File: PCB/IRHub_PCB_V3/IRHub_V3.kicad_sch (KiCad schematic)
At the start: 66 parts, among them J2 USB_C_Receptacle_USB2.0_16P, Q1 UMH3N, Q2 AO3400A, Q3 AO3400A, U1 ESP-12F, U2 CH340C, U3 AMS1117-3.3, U4 TSOP382xx, U5 ME6211C33M5

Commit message: complete schematic i think ?
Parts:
- removed OLED1: Conn_01x04_Pin, Connector_PinHeader_2.54mm:PinHeader_1x04_P2.54mm_Vertical, symbol Connector:Conn_01x04_Pin
- added 5V1: VCC, TestPoint:TestPoint_Pad_D2.0mm, symbol Connector:TestPoint
- added DispTouch: DispTouch, Connector_JST:JST_SH_BM06B-SRSS-TB_1x06-1MP_P1.00mm_Vertical, symbol Connector:Conn_01x06_Socket
- added TP9: 3V3, TestPoint:TestPoint_Pad_D2.0mm, symbol Connector:TestPoint
- added T_D+1: D+, TestPoint:TestPoint_Pad_D2.0mm, symbol Connector:TestPoint
- added T_D-1: D-, TestPoint:TestPoint_Pad_D2.0mm, symbol Connector:TestPoint
- added T_D6: D6, TestPoint:TestPoint_Pad_D2.0mm, symbol Connector:TestPoint
- added T_D7: D7, TestPoint:TestPoint_Pad_D2.0mm, symbol Connector:TestPoint
- added T_GND1: GND, TestPoint:TestPoint_Pad_D2.0mm, symbol Connector:TestPoint
- added T_RX1: RX, TestPoint:TestPoint_Pad_D2.0mm, symbol Connector:TestPoint
- added T_TX1: TX, TestPoint:TestPoint_Pad_D2.0mm, symbol Connector:TestPoint
- LS1: footprint CMT-7525-80-SMT-TR:XDCR_CMT-7525-80-SMT-TR -> CMT-7525:XDCR_CMT-7525-80-SMT-TR
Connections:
- net +3.3V: now also DispTouch.2 (Pin_2), TP9.1
- net +5V: now also 5V1.1
- net D+: now also T_D+1.1
- net D-: now also T_D-1.1
- net D0: now also DispTouch.5 (Pin_5)
- net D1: now also DispTouch.3 (Pin_3)
- net D2: now also DispTouch.4 (Pin_4)
- net D6: now also T_D6.1
- net D7: now also T_D7.1
- net GND: now also DispTouch.1 (Pin_1), DispTouch.6 (Pin_6), T_GND1.1
- net RX: now also T_RX1.1
- net TX: now also T_TX1.1
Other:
- moved on the sheet: D31, D32, D33, D34, D35, D36, D37, D38, R10, R11, R12, R13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

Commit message: final design i think
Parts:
- removed D32, D33, D34, D35, D36, D37, D38: IR204A, LED_THT:LED_D3.0mm_IRBlack, symbol LED:IR204A
- added IR_L2, IR_L3, IR_L4, IR_L5, IR_L6, IR_L7, IR_L8: IR204A, LED_THT:LED_D3.0mm_IRBlack, symbol LED:IR204A
- added R16, R17, R18: 12000, Resistor_SMD:R_1206_3216Metric_Pad1.30x1.75mm_HandSolder, symbol Device:R
- added SW1: SW_Push, Button_Switch_SMD:SW_SPST_TS-1088-xR020, symbol Switch:SW_Push
- BZR1: renamed from LS1; value CMT-7525-80-SMT-TR -> CMT-7525
- R6: value 5100 -> 12000
- renumbered U3 to AMS1117, U2 to CH340C1, DispTouch to DispTouch1, U1 to ESP1, D31 to IR_L1, U4 to IR_RECV1, U5 to ME6211, Q3 to MFT1, Q2 to MFT2, J2 to USB1
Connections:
- net +3.3V: now also R17.2, R18.2
- net D3: now also R15.2; no longer R15.1
- net D4: now also R18.1
- net D8: now also R16.1
- net GND: now also R16.2, SW1.2
- net IR_GND: now also IR_L2.1 (K), IR_L3.1 (K), IR_L4.1 (K), IR_L5.1 (K), IR_L6.1 (K), IR_L7.1 (K), IR_L8.1 (K)
- net RST: now also R17.1, SW1.1
- net at R13.1: now also IR_L7.2 (A)
- net at R8.1: now also IR_L2.2 (A)
- net at R11.1: now also IR_L5.2 (A)
- net at R10.1: now also IR_L4.2 (A)
- net at R9.1: now also IR_L3.2 (A)
- net at MFT1.1 (G): now also R15.1; no longer R15.2
- net at R12.1: now also IR_L6.2 (A)
- net at R14.1: now also IR_L8.2 (A)
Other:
- moved on the sheet: 5V1, AMS1117, BZR1, C3, C4, CH340C1, DispTouch1, ESP1, IR_L1, IR_RECV1, ME6211, MFT1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

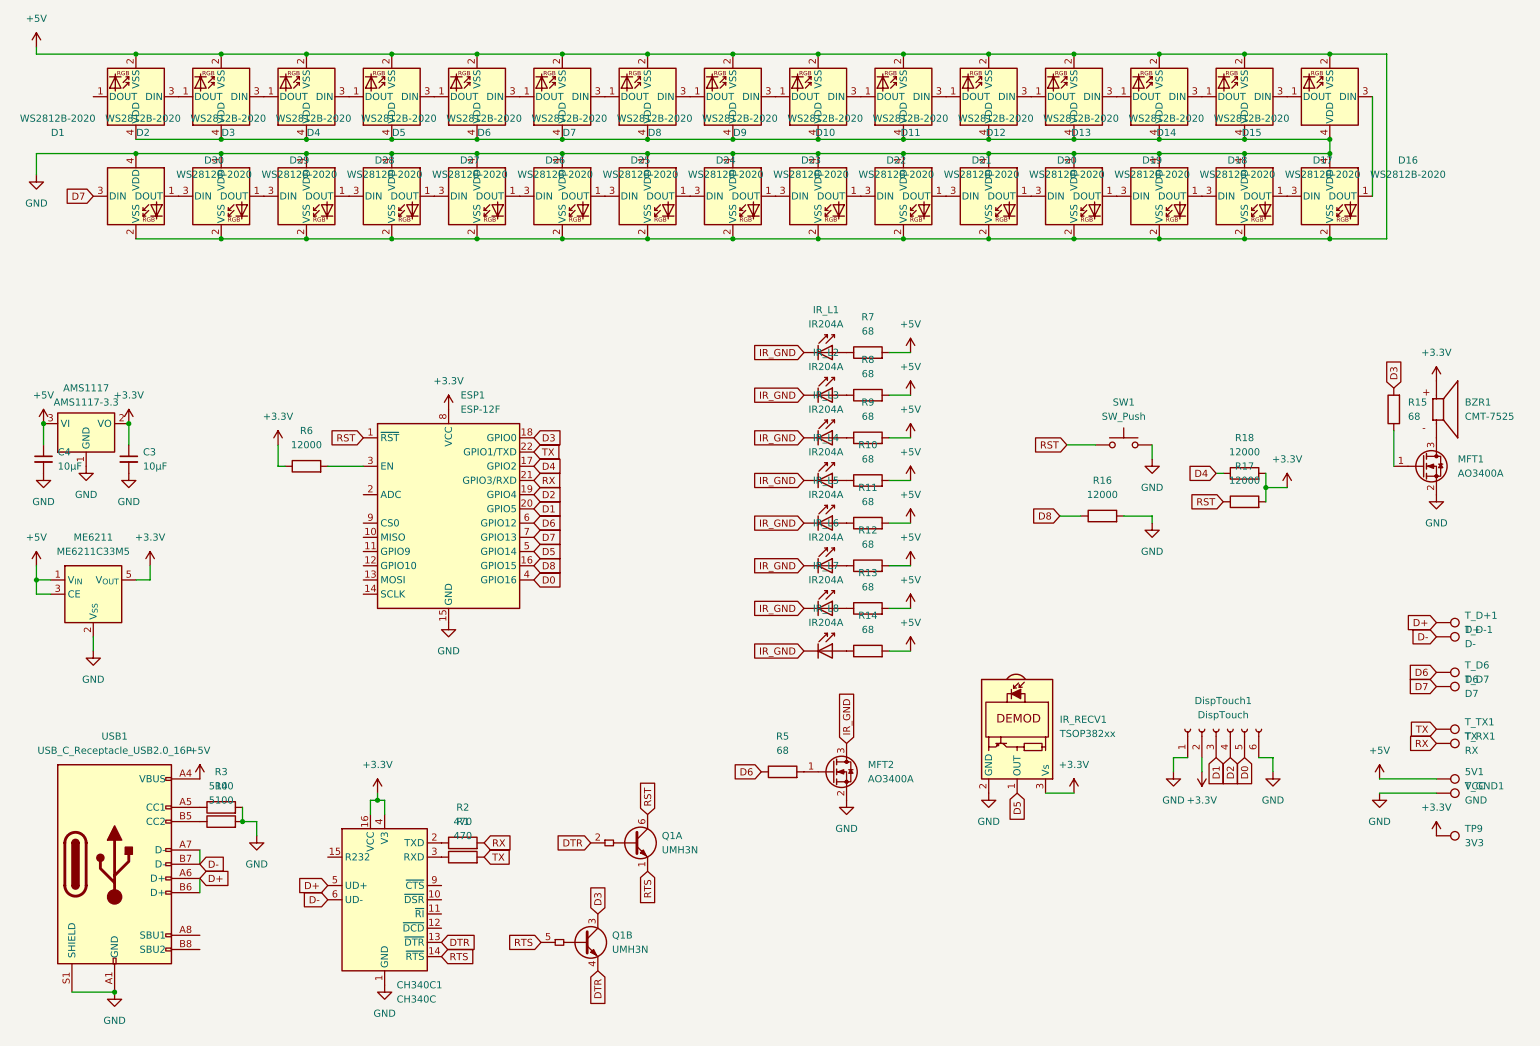
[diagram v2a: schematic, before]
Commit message: added haptics
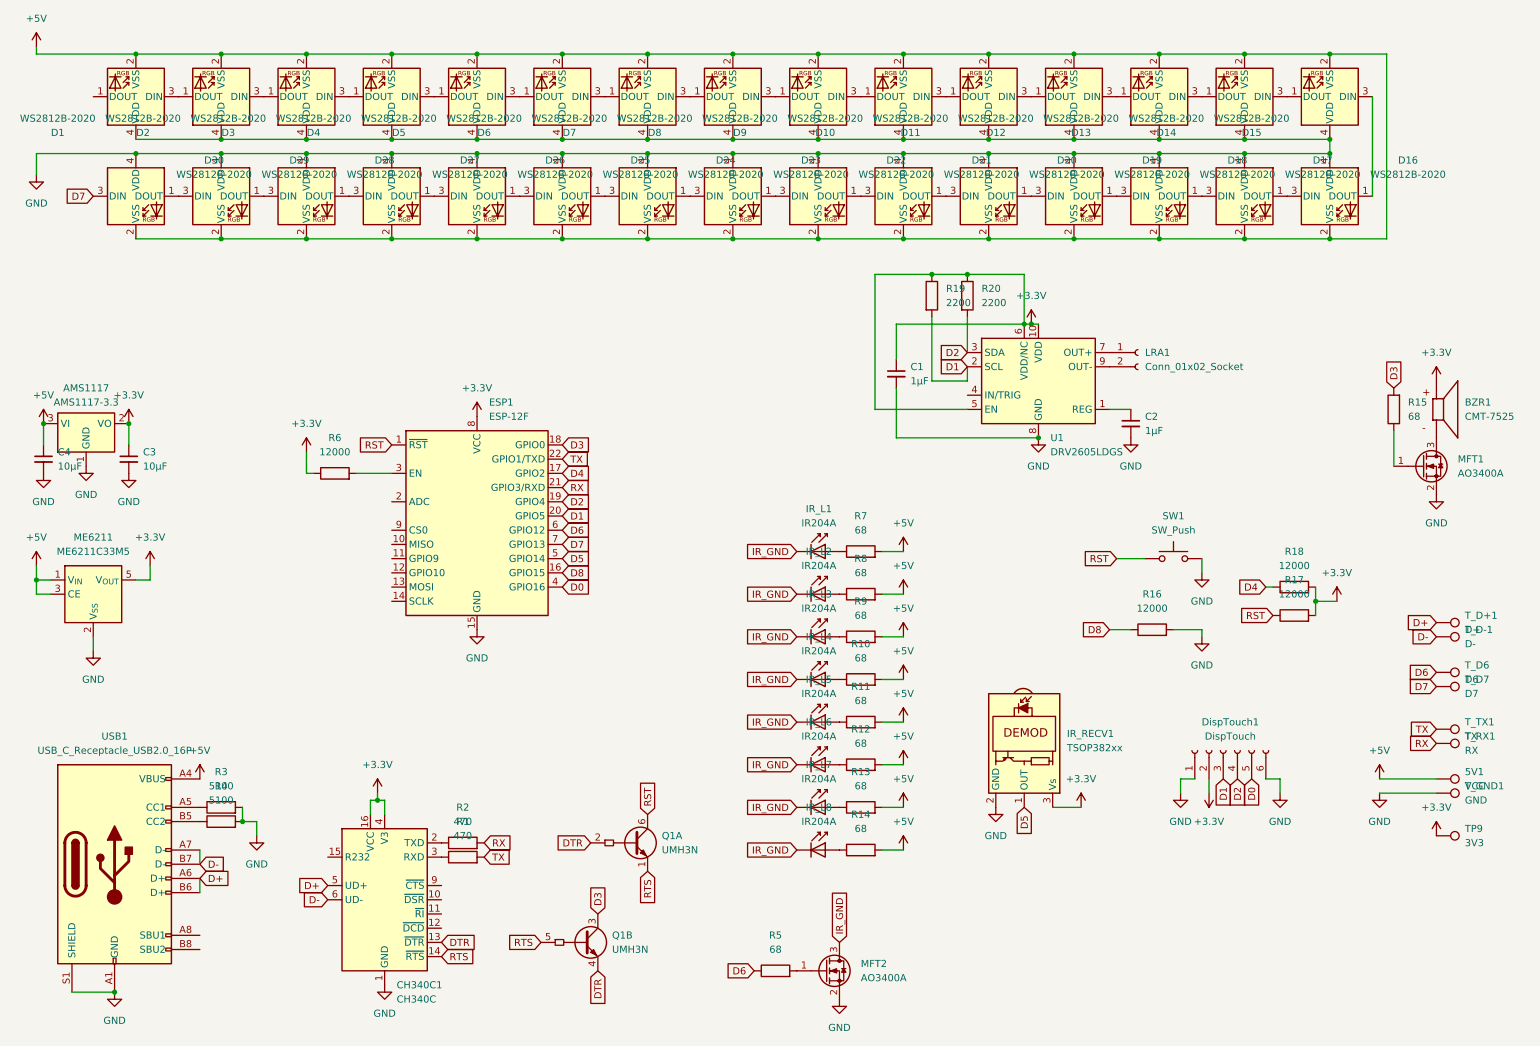
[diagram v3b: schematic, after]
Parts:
- added C1, C2: 1µF, Capacitor_SMD:C_0805_2012Metric_Pad1.18x1.45mm_HandSolder, symbol Device:C_Small
- added LRA1: Conn_01x02_Socket, Connector_PinHeader_2.00mm:PinHeader_1x02_P2.00mm_Vertical, symbol Connector:Conn_01x02_Socket
- added R19, R20: 2200, Resistor_SMD:R_0805_2012Metric_Pad1.20x1.40mm_HandSolder, symbol Device:R
- added U1: DRV2605LDGS, Package_SO:VSSOP-10_3x3mm_P0.5mm, symbol Driver_Haptic:DRV2605LDGS
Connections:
- net +3.3V: now also C1.1, R19.1, R20.1, U1.10 (VDD), U1.5 (EN), U1.6 (VDD/NC)
- net D1: now also R19.2, U1.2 (SCL)
- net D2: now also R20.2, U1.3 (SDA)
- net GND: now also C1.2, C2.2, U1.8 (GND)
- new net: C2.1, U1.1 (REG)
- new net: LRA1.1 (Pin_1), U1.7 (OUT+)
- new net: LRA1.2 (Pin_2), U1.9 (OUT-)
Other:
- moved on the sheet: DispTouch1, ESP1, IR_L1, IR_L2, IR_L3, IR_L4, IR_L5, IR_L6, IR_L7, IR_L8, IR_RECV1, MFT2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

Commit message: power pcb done
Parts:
- 5V1, TP9, T_D+1, T_D-1, T_D6, T_D7, T_GND1, T_RX1, T_TX1: footprint TestPoint:TestPoint_Pad_D2.0mm -> TestPoint:TestPoint_Pad_D1.0mm
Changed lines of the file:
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@@
 			)
 		)
-		(property "Footprint" "TestPoint:TestPoint_Pad_D2.0mm"
+		(property "Footprint" "TestPoint:TestPoint_Pad_D1.0mm"
 			(at 267.97 156.21 0)
 			(effects
@@
 			)
 		)
-		(property "Footprint" "TestPoint:TestPoint_Pad_D2.0mm"
+		(property "Footprint" "TestPoint:TestPoint_Pad_D1.0mm"
 			(at 267.97 130.81 0)
 			(effects
@@
 			)
 		)
-		(property "Footprint" "TestPoint:TestPoint_Pad_D2.0mm"
+		(property "Footprint" "TestPoint:TestPoint_Pad_D1.0mm"
 			(at 267.97 149.86 0)
 			(effects
@@
 			)
 		)
-		(property "Footprint" "TestPoint:TestPoint_Pad_D2.0mm"
+		(property "Footprint" "TestPoint:TestPoint_Pad_D1.0mm"
 			(at 267.97 128.27 0)
 			(effects
@@
 			)
 		)
-		(property "Footprint" "TestPoint:TestPoint_Pad_D2.0mm"
+		(property "Footprint" "TestPoint:TestPoint_Pad_D1.0mm"
 			(at 267.97 147.32 0)
 			(effects
@@
 			)
 		)
-		(property "Footprint" "TestPoint:TestPoint_Pad_D2.0mm"
+		(property "Footprint" "TestPoint:TestPoint_Pad_D1.0mm"
 			(at 267.97 166.37 0)
 			(effects
@@
 			)
 		)
-		(property "Footprint" "TestPoint:TestPoint_Pad_D2.0mm"
+		(property "Footprint" "TestPoint:TestPoint_Pad_D1.0mm"
 			(at 267.97 158.75 0)
 			(effects
@@
 			)
 		)
-		(property "Footprint" "TestPoint:TestPoint_Pad_D2.0mm"
+		(property "Footprint" "TestPoint:TestPoint_Pad_D1.0mm"
 			(at 267.97 137.16 0)
 			(effects
@@
 			)
 		)
-		(property "Footprint" "TestPoint:TestPoint_Pad_D2.0mm"
+		(property "Footprint" "TestPoint:TestPoint_Pad_D1.0mm"
 			(at 267.97 139.7 0)
 			(effects

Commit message: finished placement
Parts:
- removed ME6211: ME6211C33M5, Package_TO_SOT_SMD:SOT-23-5, symbol Regulator_Linear:ME6211C33M5
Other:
- moved on the sheet: AMS1117, C3, C4

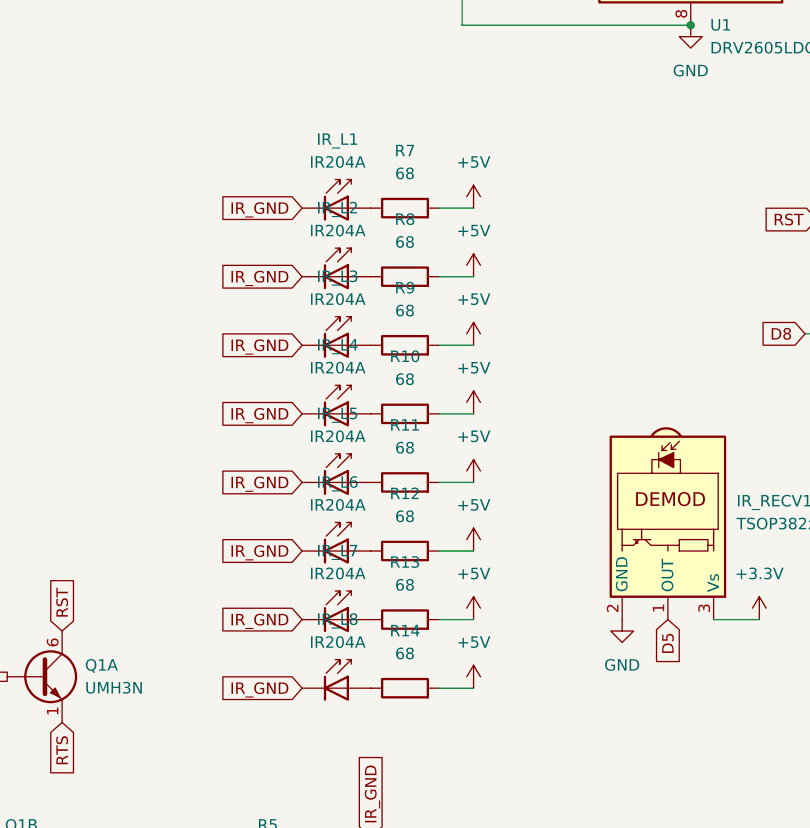
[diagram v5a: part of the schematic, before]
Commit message: update resistor values
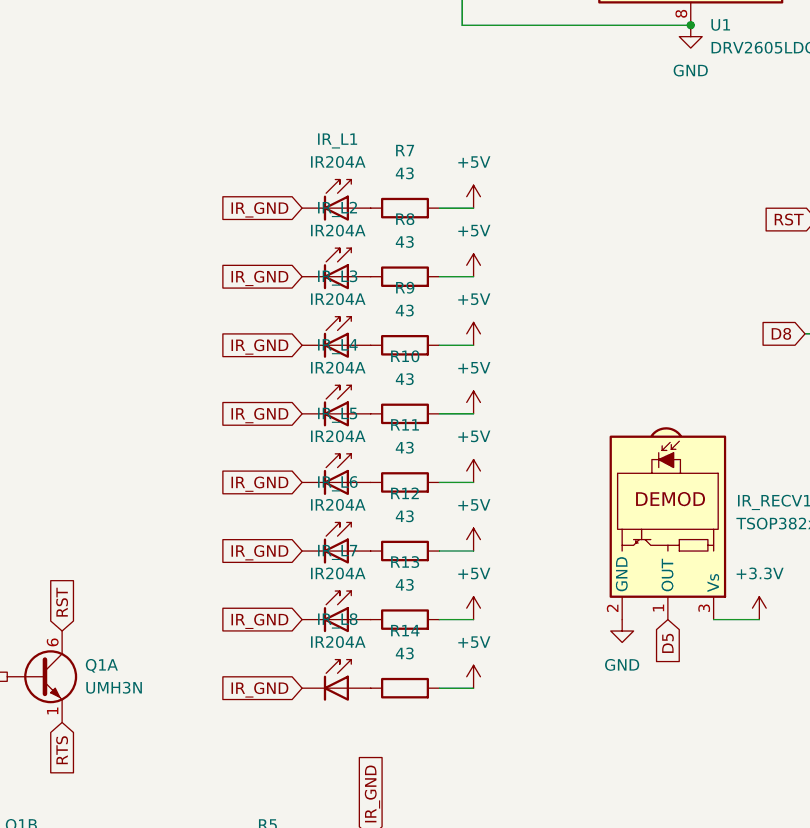
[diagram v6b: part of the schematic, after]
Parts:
- R10, R11, R12, R13, R14, R7, R8, R9: value 68 -> 43; footprint Resistor_SMD:R_1206_3216Metric_Pad1.30x1.75mm_HandSolder -> Resistor_SMD:R_1210_3225Metric_Pad1.30x2.65mm_HandSolder
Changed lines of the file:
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@@
 			)
 		)
-		(property "Value" "68"
+		(property "Value" "43"
 			(at 165.1 137.16 90)
 			(effects
@@
 			)
 		)
-		(property "Footprint" "Resistor_SMD:R_1206_3216Metric_Pad1.30x1.75mm_HandSolder"
+		(property "Footprint" "Resistor_SMD:R_1210_3225Metric_Pad1.30x2.65mm_HandSolder"
 			(at 165.1 142.748 90)
 			(effects
@@
 			)
 		)
-		(property "Value" "68"
+		(property "Value" "43"
 			(at 165.1 121.92 90)
 			(effects
@@
 			)
 		)
-		(property "Footprint" "Resistor_SMD:R_1206_3216Metric_Pad1.30x1.75mm_HandSolder"
+		(property "Footprint" "Resistor_SMD:R_1210_3225Metric_Pad1.30x2.65mm_HandSolder"
 			(at 165.1 127.508 90)
 			(effects
@@
 			)
 		)
-		(property "Value" "68"
+		(property "Value" "43"
 			(at 165.1 144.78 90)
 			(effects
@@
 			)
 		)
-		(property "Footprint" "Resistor_SMD:R_1206_3216Metric_Pad1.30x1.75mm_HandSolder"
+		(property "Footprint" "Resistor_SMD:R_1210_3225Metric_Pad1.30x2.65mm_HandSolder"
 			(at 165.1 150.368 90)
 			(effects
@@
 			)
 		)
-		(property "Value" "68"
+		(property "Value" "43"
 			(at 165.1 106.68 90)
 			(effects
@@
 			)
 		)
-		(property "Footprint" "Resistor_SMD:R_1206_3216Metric_Pad1.30x1.75mm_HandSolder"
+		(property "Footprint" "Resistor_SMD:R_1210_3225Metric_Pad1.30x2.65mm_HandSolder"
 			(at 165.1 112.268 90)
 			(effects
@@
 			)
 		)
-		(property "Value" "68"
+		(property "Value" "43"
 			(at 165.1 152.4 90)
 			(effects
@@
 			)
 		)
-		(property "Footprint" "Resistor_SMD:R_1206_3216Metric_Pad1.30x1.75mm_HandSolder"
+		(property "Footprint" "Resistor_SMD:R_1210_3225Metric_Pad1.30x2.65mm_HandSolder"
 			(at 165.1 157.988 90)
 			(effects
@@
 			)
 		)
-		(property "Value" "68"
+		(property "Value" "43"
 			(at 165.1 129.54 90)
 			(effects
@@
 			)
 		)
-		(property "Footprint" "Resistor_SMD:R_1206_3216Metric_Pad1.30x1.75mm_HandSolder"
+		(property "Footprint" "Resistor_SMD:R_1210_3225Metric_Pad1.30x2.65mm_HandSolder"
 			(at 165.1 135.128 90)
 			(effects
@@
 			)
 		)
-		(property "Value" "68"
+		(property "Value" "43"
 			(at 165.1 114.3 90)
 			(effects
@@
 			)
 		)
-		(property "Footprint" "Resistor_SMD:R_1206_3216Metric_Pad1.30x1.75mm_HandSolder"
+		(property "Footprint" "Resistor_SMD:R_1210_3225Metric_Pad1.30x2.65mm_HandSolder"
 			(at 165.1 119.888 90)
 			(effects
@@
 			)
 		)
-		(property "Value" "68"
+		(property "Value" "43"
 			(at 165.1 160.02 90)
 			(effects
@@
 			)
 		)
-		(property "Footprint" "Resistor_SMD:R_1206_3216Metric_Pad1.30x1.75mm_HandSolder"
+		(property "Footprint" "Resistor_SMD:R_1210_3225Metric_Pad1.30x2.65mm_HandSolder"
 			(at 165.1 165.608 90)
 			(effects

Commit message: final board design i hope
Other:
- company: (none) -> Madhukar Temba
- title: (none) -> IR Hub
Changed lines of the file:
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@@
 	(generator_version "9.0")
 	(paper "A4")
+	(title_block
+		(title "IR Hub")
+		(date "2025-09-15")
+		(rev "3")
+		(company "Madhukar Temba")
+	)
 	(junction
 		(at 195.58 69.85)

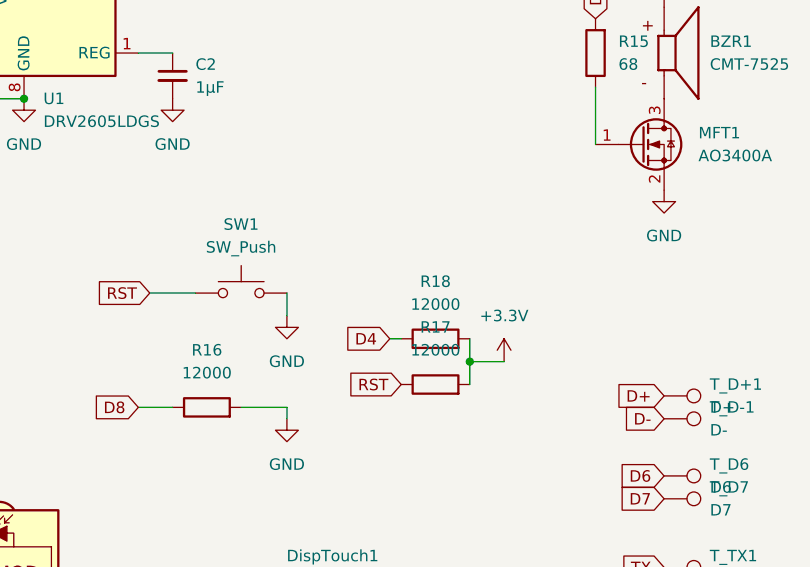
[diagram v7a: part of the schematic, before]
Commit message: added one missing res 👀
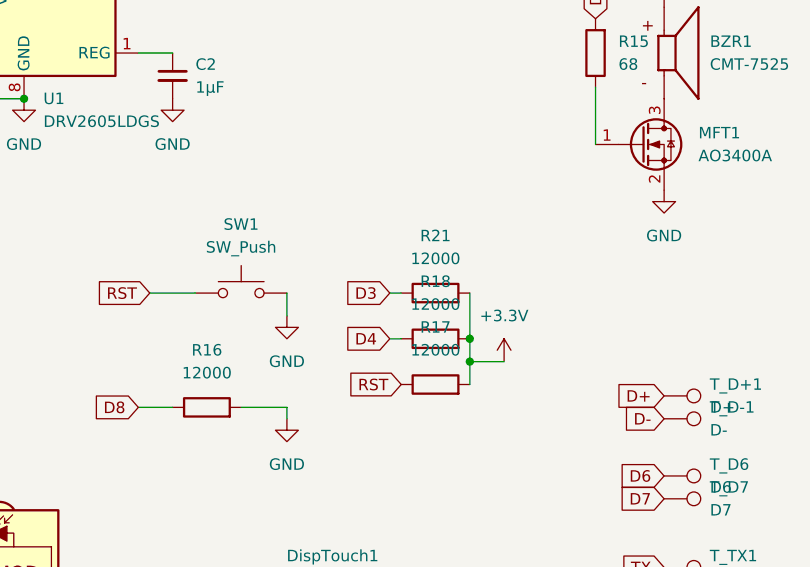
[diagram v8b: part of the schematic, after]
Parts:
- added R21: 12000, Resistor_SMD:R_1206_3216Metric_Pad1.30x1.75mm_HandSolder, symbol Device:R
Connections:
- net +3.3V: now also R21.2
- net D3: now also R21.1
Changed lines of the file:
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@@
 	)
 	(junction
+		(at 246.38 116.84)
+		(diameter 0)
+		(color 0 0 0 0)
+	)
+	(junction
 		(at 78.74 154.94)
 		(diameter 0)
@@
 	(wire
 		(pts
+			(xy 237.49 111.76) (xy 238.76 111.76)
+		)
+		(stroke
+			(width 0)
+			(type default)
+		)
+	)
+	(wire
+		(pts
 			(xy 50.8 36.83) (xy 66.04 36.83)
 		)
@@
 	(wire
 		(pts
+			(xy 246.38 111.76) (xy 246.38 116.84)
+		)
+		(stroke
+			(width 0)
+			(type default)
+		)
+	)
+	(wire
+		(pts
 			(xy 111.76 21.59) (xy 127 21.59)
 		)
@@
 		)
 	)
+	(global_label "D3"
+		(shape input)
+		(at 237.49 111.76 180)
+		(fields_autoplaced yes)
+		(effects
+			(font
+				(size 1.27 1.27)
+			)
+			(justify right)
+		)
+		(property "Intersheetrefs" "${INTERSHEET_REFS}"
+			(at 232.0253 111.76 0)
+			(effects
+				(font
+					(size 1.27 1.27)
+				)
+				(justify right)
+				(hide yes)
+			)
+		)
+	)
 	(global_label "RTS"
 		(shape input)
@@
 					(unit 1)
 				)
+			)
+		)
+	)
+	(symbol
+		(lib_id "Device:R")
+		(at 242.57 111.76 90)
+		(unit 1)
+		(exclude_from_sim no)
+		(in_bom yes)
+		(on_board yes)
+		(dnp no)
+		(fields_autoplaced yes)
+		(property "Reference" "R21"
+			(at 242.57 105.41 90)
+			(effects
+				(font
+					(size 1.27 1.27)
+				)
+			)
+		)
+		(property "Value" "12000"
+			(at 242.57 107.95 90)
+			(effects
+				(font
+					(size 1.27 1.27)
+				)
+			)
+		)
+		(property "Footprint" "Resistor_SMD:R_1206_3216Metric_Pad1.30x1.75mm_HandSolder"
+			(at 242.57 113.538 90)
+			(effects
+				(font
+					(size 1.27 1.27)
+				)
+				(hide yes)
+			)
+		)
+		(property "Datasheet" "~"
+			(at 242.57 111.76 0)
+			(effects
+				(font
+					(size 1.27 1.27)
+				)
+				(hide yes)
+			)
+		)
+		(property "Description" "Resistor"
+			(at 242.57 111.76 0)
+			(effects
+				(font
+					(size 1.27 1.27)
+				)
+				(hide yes)
+			)
+		)
+		(pin "1"
+		)
+		(pin "2"
+		)
+		(instances
+			(project "IRHub_V3"
+				(path "/aae96d67-430c-4b50-8ebf-3dca81de3bb1"
+					(reference "R21")
+					(unit 1)
+				)
